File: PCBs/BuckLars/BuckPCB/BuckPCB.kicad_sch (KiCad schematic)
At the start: 56 parts, among them J1 Program_header, J2 Main board header, J3 12V, J4 5V, Q1 IRLIZ44N, Q2 IRLIZ44N, Q3 IRLIZ44N, Q4 IRLIZ44N, SW1 RESET, SW2 Boot, U1 ESP32-WROOM-32D, U2 LT1936, U3 LF2304NTR, U4 LF2304NTR

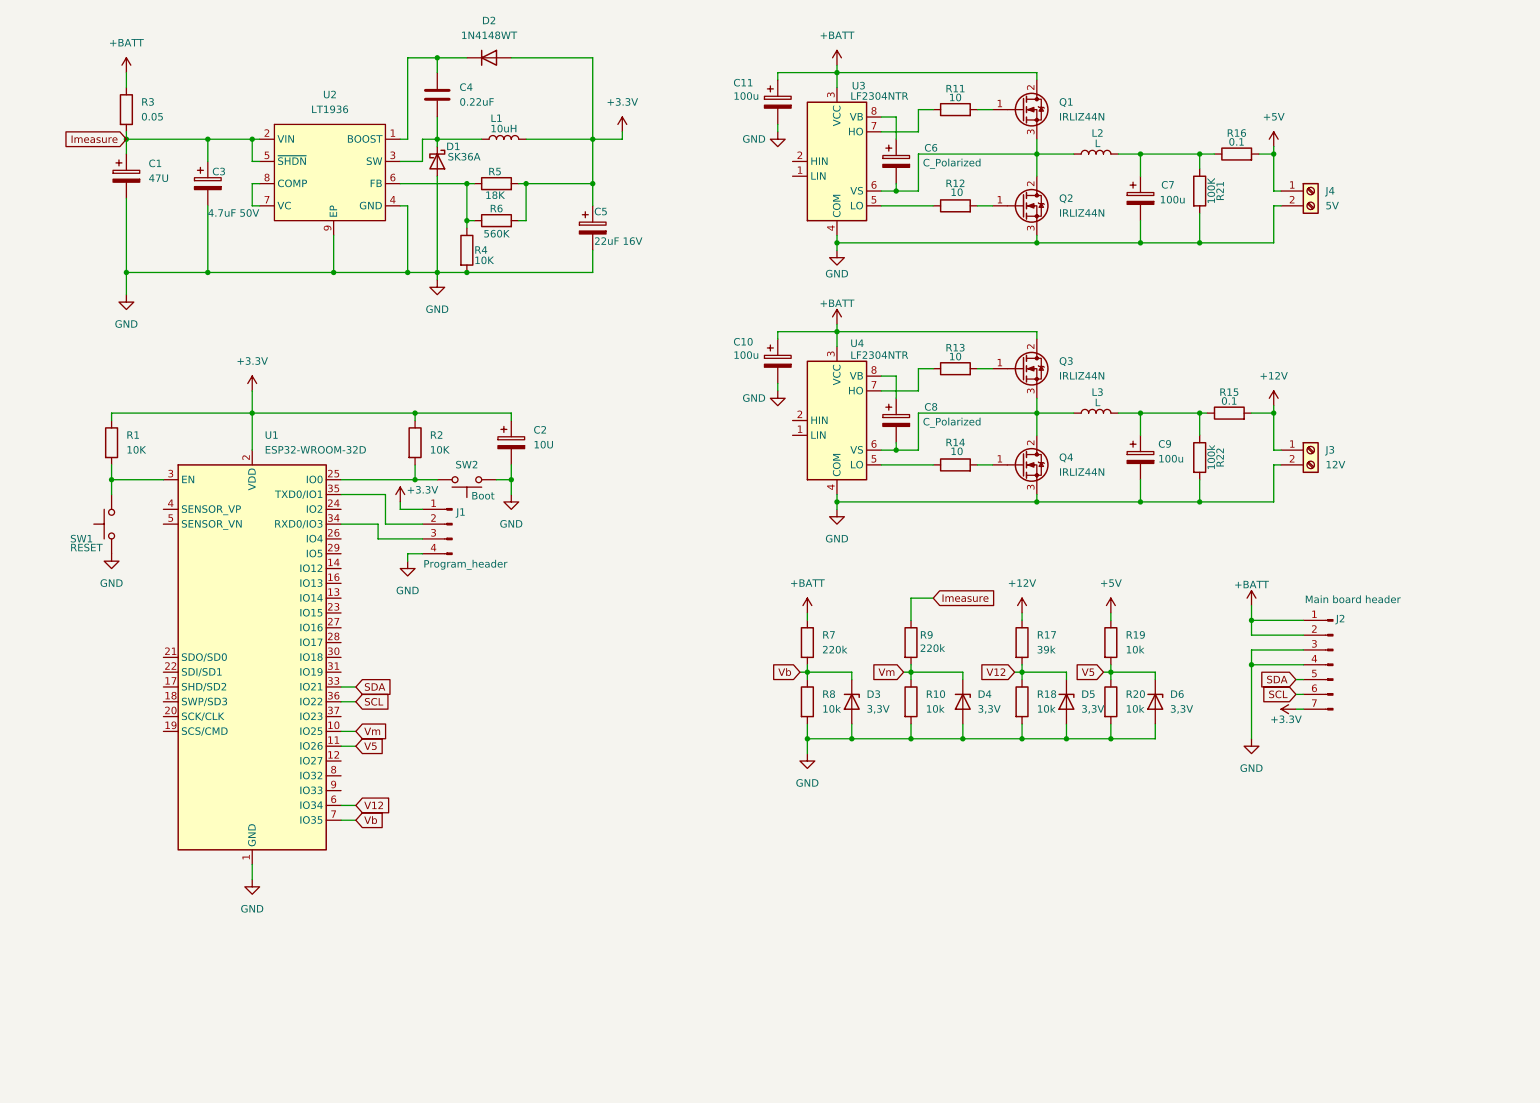
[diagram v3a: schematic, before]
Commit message: wired buck converter pcb
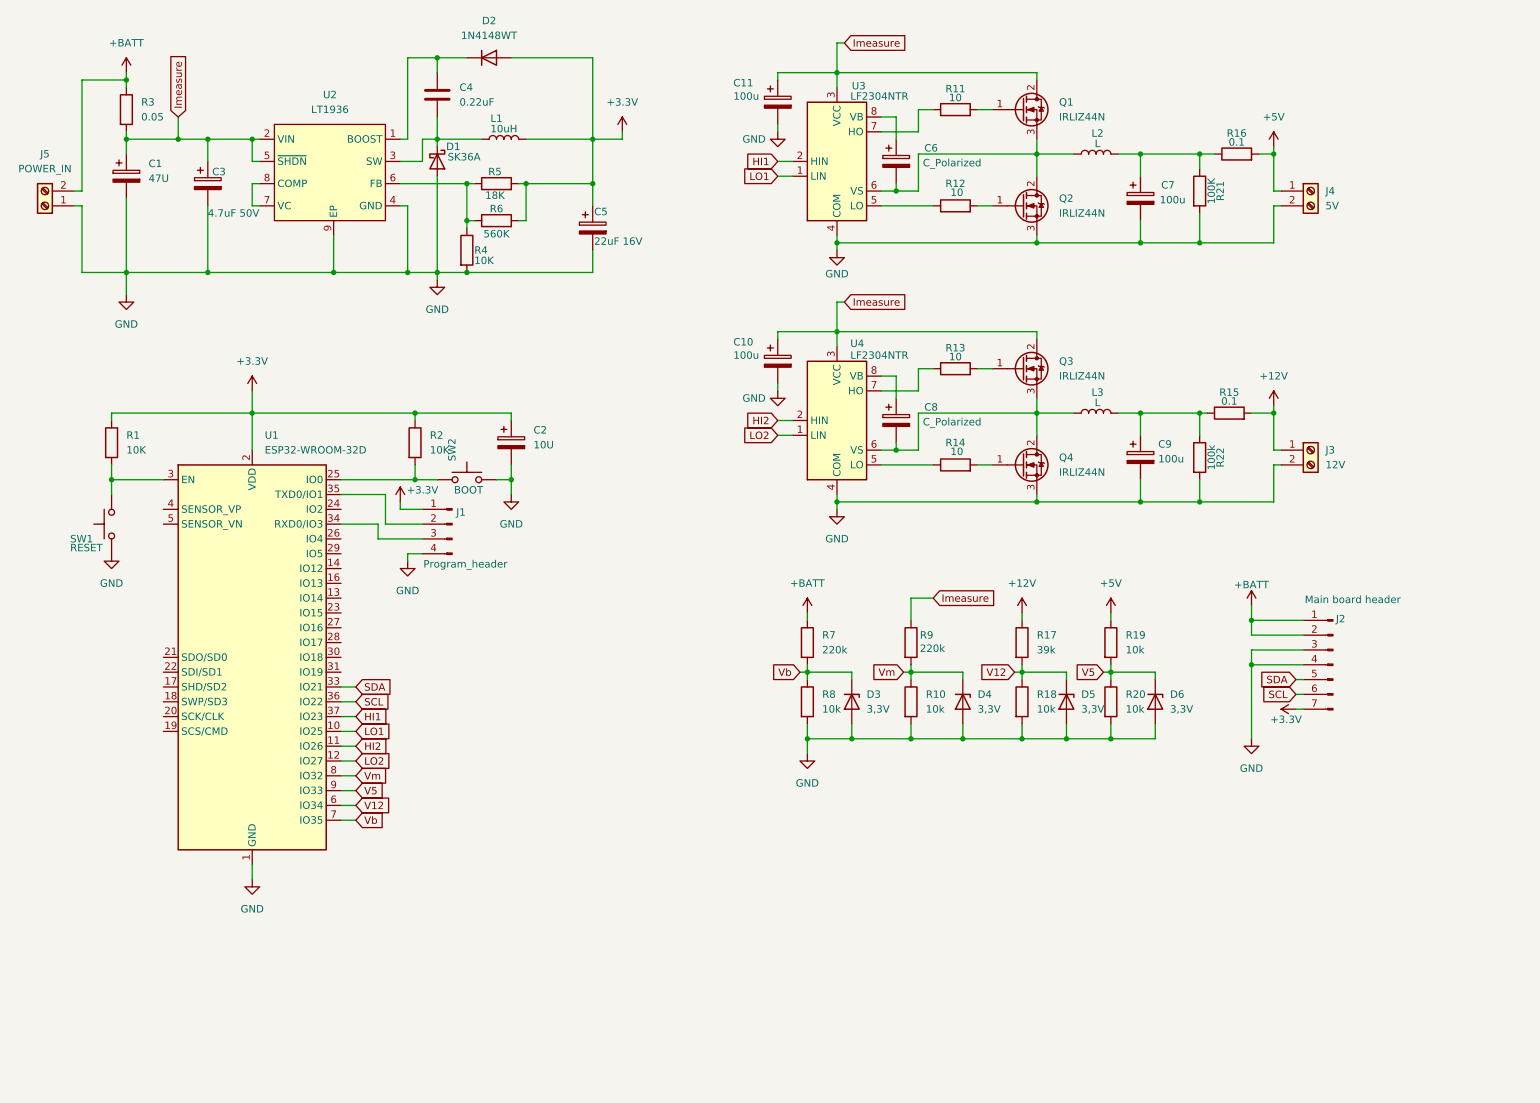
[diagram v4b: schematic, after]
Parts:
- added J5: POWER_IN, TerminalBlock:TerminalBlock_MaiXu_MX126-5.0-02P_1x02_P5.00mm, symbol Connector:Screw_Terminal_01x02
- C6, C8: footprint Capacitor_SMD:CP_Elec_8x10.5 -> Capacitor_SMD:CP_Elec_5x5.4
- SW2: value Boot -> BOOT
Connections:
- net +BATT: now also J5.2 (Pin_2); no longer C10.1, C11.1, Q1.2 (D), Q3.2 (D), U3.3 (VCC), U4.3 (VCC)
- net GND: now also J5.1 (Pin_1); no longer SW1.2 (A), SW2.1 (A)
- net Imeasure: now also C10.1, C11.1, Q1.2 (D), Q3.2 (D), U3.3 (VCC), U4.3 (VCC)
- net V5: now also U1.9 (IO33); no longer U1.11 (IO26)
- net Vm: now also U1.8 (IO32); no longer U1.10 (IO25)
- net LO2: now reaches U1.12 (IO27)
- net LO2: now also U4.1 (LIN)
- net at R2.2, U1.25 (IO0): now also SW2.1 (A); no longer SW2.3 (B), SW2.4 (B)
- net at R1.2, U1.3 (EN): now also SW1.2 (B); no longer SW1.3 (B), SW1.4 (B)
- net HI1: now reaches U1.37 (IO23)
- net HI1: now also U3.2 (HIN)
- net HI2: now reaches U4.2 (HIN)
- net HI2: now also U1.11 (IO26)
- net LO1: now reaches U3.1 (LIN)
- net LO1: now also U1.10 (IO25)

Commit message: layout changes schematic
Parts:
- added R23: 10K, Resistor_SMD:R_1206_3216Metric_Pad1.30x1.75mm_HandSolder, symbol Device:R
- added R24, R25: 4k7, Resistor_SMD:R_1206_3216Metric_Pad1.30x1.75mm_HandSolder, symbol Device:R
- C4: symbol Device:C -> Device:C_Polarized
- C6, C8: value C_Polarized -> 100n
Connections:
- net +3.3V: now also R23.1, R24.1, R25.1
- net +BATT: no longer J2.1 (Pin_1), J2.2 (Pin_2)
- net Imeasure: now also J2.1 (Pin_1), J2.2 (Pin_2)
- net SCL: now also R25.2
- net SDA: now also R24.2
- net at J1.2 (Pin_2), U1.35 (TXD0/IO1): now also R23.2
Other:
- moved on the sheet: C7, C9, J1, L2, L3, Q1, Q3, R11, R13, R15, R16, R21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

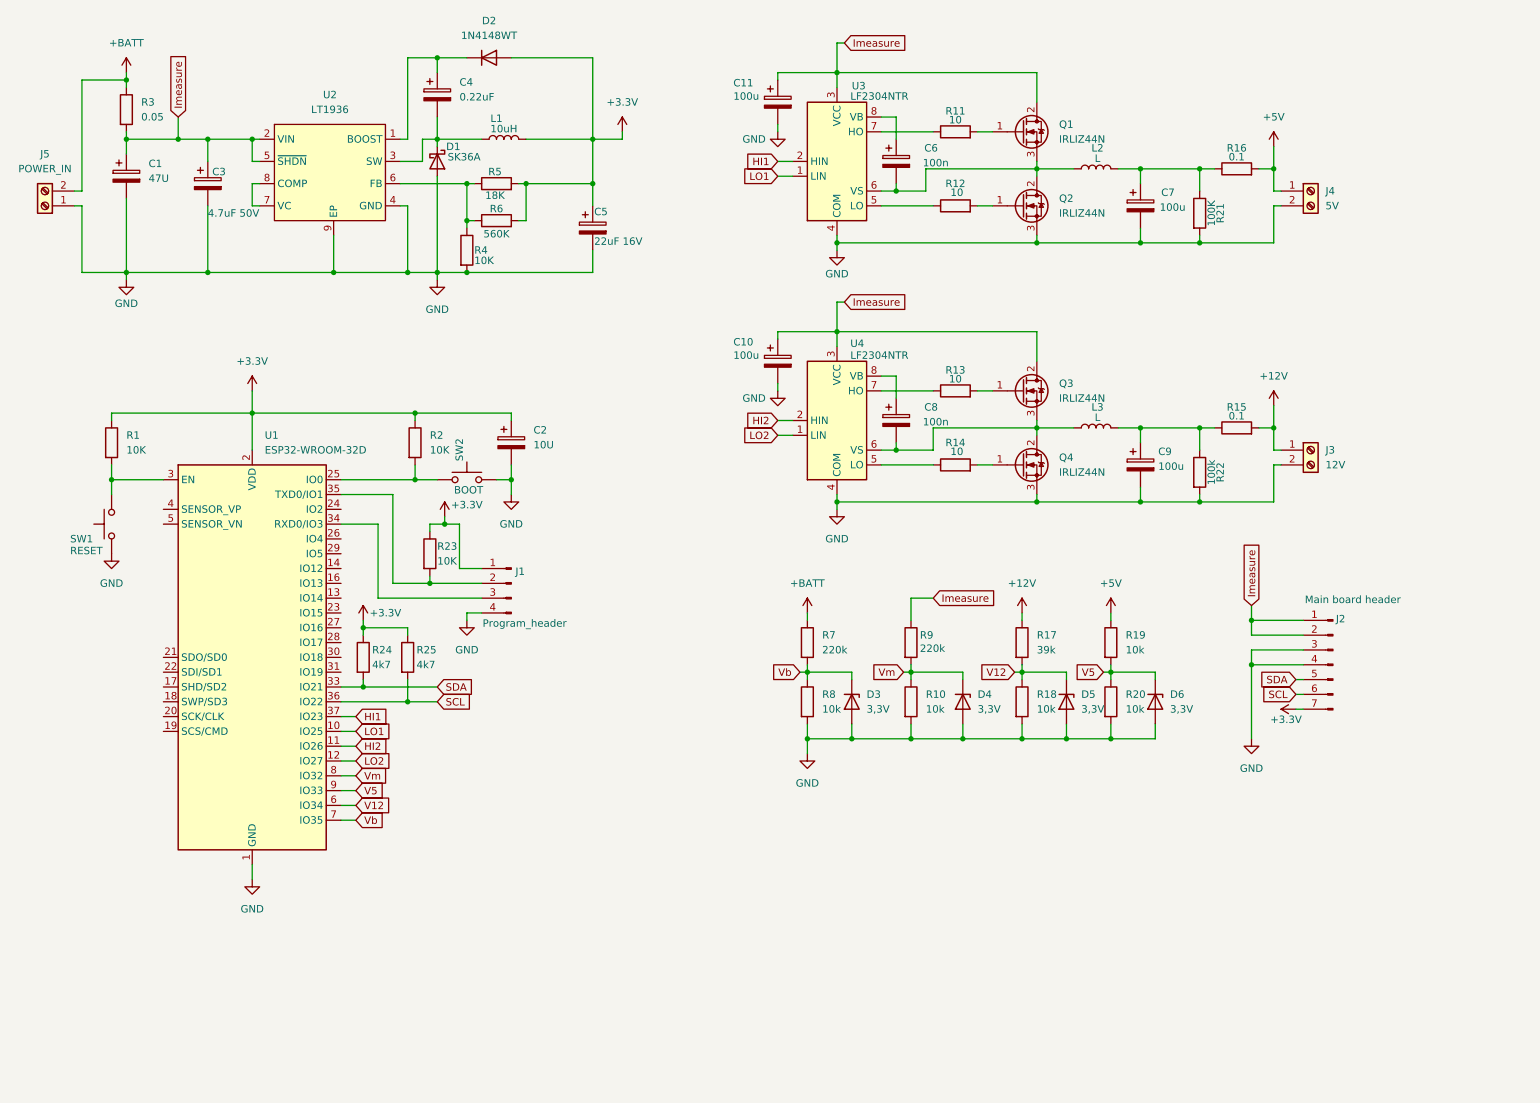
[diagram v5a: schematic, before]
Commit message: changed footprints buck
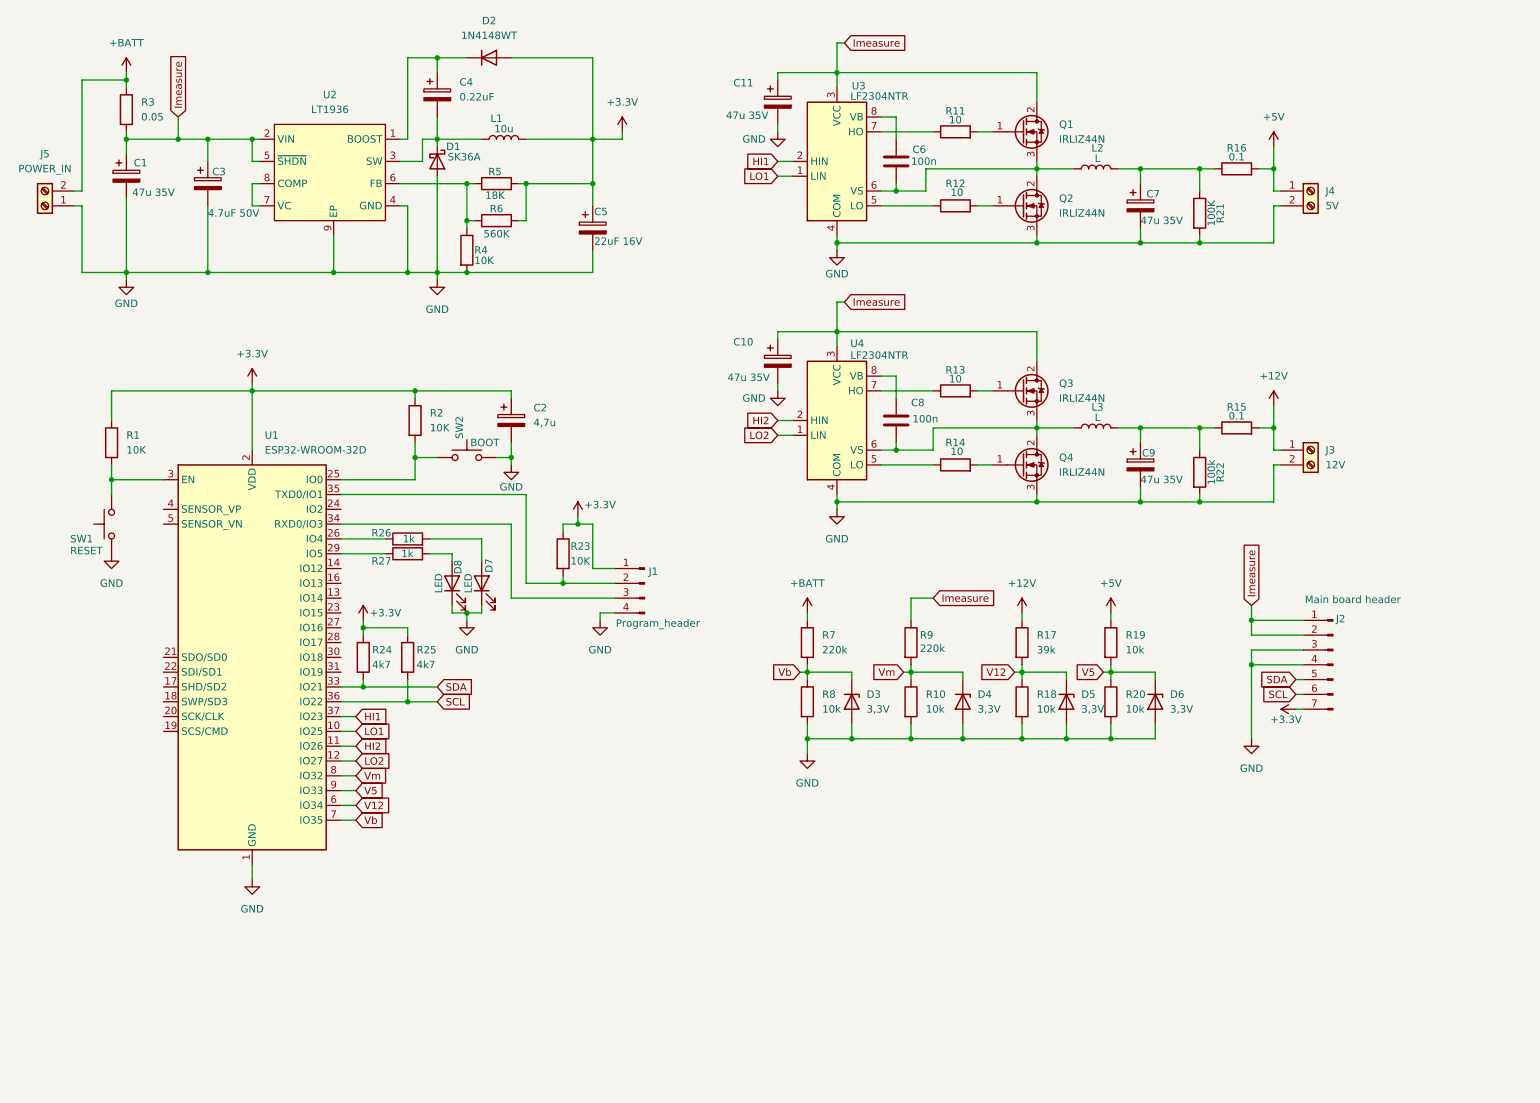
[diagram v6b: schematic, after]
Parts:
- removed C6, C8: 100n, Capacitor_SMD:CP_Elec_5x5.4, symbol Device:C_Polarized
- added C6, C8: 100n, Capacitor_SMD:C_1206_3216Metric_Pad1.33x1.80mm_HandSolder, symbol Device:C
- added D7, D8: LED, LED_SMD:LED_0805_2012Metric, symbol Device:LED
- added R26, R27: 1k, Resistor_SMD:R_1206_3216Metric_Pad1.30x1.75mm_HandSolder, symbol Device:R
- C1: value 47U -> 47u 35V; footprint Capacitor_SMD:CP_Elec_4x5.3 -> Capacitor_SMD:CP_Elec_6.3x5.7
- C10, C11, C7, C9: value 100u -> 47u 35V; footprint Capacitor_SMD:CP_Elec_8x10.5 -> Capacitor_SMD:CP_Elec_6.3x5.7
- C2: value 10U -> 4,7u
- D1: footprint Diode_SMD:D_SMC -> Diode_SMD:D_SMC-RM10_Universal_Handsoldering
- L1: value 10uH -> 10u
- SW1, SW2: footprint Button_Switch_SMD:SW_SPST_CK_RS282G05A3 -> Button_Switch_SMD:SW_Tactile_SPST_NO_Straight_CK_PTS636Sx25SMTRLFS
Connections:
- net GND: now also D7.1 (K), D8.1 (K)
- net at U1.26 (IO4): now also R26.1
- net at U1.29 (IO5): now also R27.1
- net at L3.1, Q3.3 (S), Q4.2 (D)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: now also C8.2
- net at U4.8 (VB): now also C8.1
- net at L2.1, Q1.3 (S), Q2.2 (D)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: now also C6.2
- net at U3.8 (VB): now also C6.1
- new net: D7.2 (A), R26.2
- new net: D8.2 (A), R27.2
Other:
- moved on the sheet: C2, J1, R2, R23, SW2

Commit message: wired second buck converter
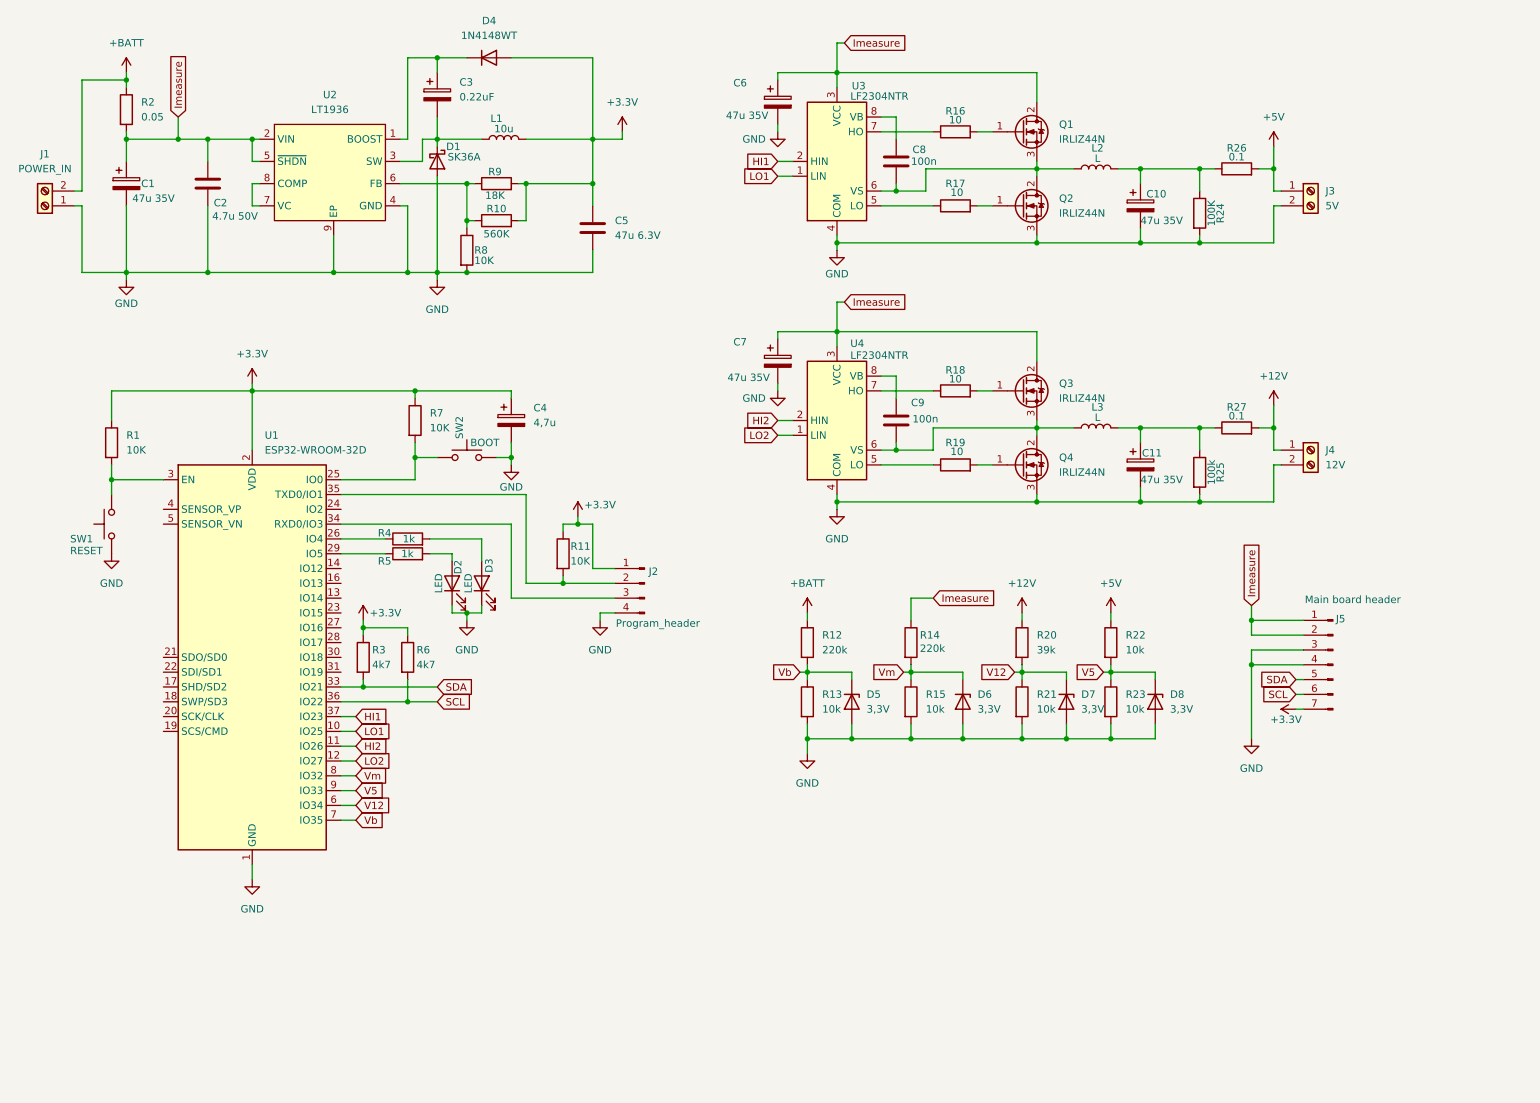
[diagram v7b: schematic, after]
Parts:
- removed C3: 4.7uF 50V, Capacitor_SMD:CP_Elec_4x5.4, symbol Device:C_Polarized
- removed C5: 22uF 16V, Capacitor_Tantalum_SMD:CP_EIA-3528-12_Kemet-T_HandSolder, symbol Device:C_Polarized
- added C2: 4.7u 50V, Diode_SMD:D_1206_3216Metric_Pad1.42x1.75mm_HandSolder, symbol Device:C
- added C5: 47u 6.3V, Diode_SMD:D_1206_3216Metric_Pad1.42x1.75mm_HandSolder, symbol Device:C
- L2, L3: footprint Inductor_SMD:L_2512_6332Metric_Pad1.52x3.35mm_HandSolder -> Inductor_SMD:L_7.3x7.3_H4.5
- renumbered C7 to C10, C9 to C11, C4 to C3, C2 to C4, C11 to C6, C10 to C7, C6 to C8, C8 to C9, D8 to D2, D7 to D3, D2 to D4, D3 to D5, D4 to D6, D5 to D7, D6 to D8, J5 to J1, J1 to J2, J4 to J3, J3 to J4, J2 to J5, R6 to R10, R23 to R11, R7 to R12, R8 to R13, R9 to R14, R10 to R15, R11 to R16, R12 to R17, R13 to R18, R14 to R19, R3 to R2, R17 to R20, R18 to R21, R19 to R22, R20 to R23, R21 to R24, R22 to R25, R16 to R26, R15 to R27, R24 to R3, R26 to R4, R27 to R5, R25 to R6, R2 to R7, R4 to R8, R5 to R9
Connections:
- net +3.3V: now also C5.1
- net GND: now also C2.2, C5.2
- net Imeasure: now also C2.1
